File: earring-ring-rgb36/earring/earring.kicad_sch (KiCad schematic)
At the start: 44 parts, among them J1 Conn_01x04, SW1 SW_Push, U2 STM32L031G6Ux

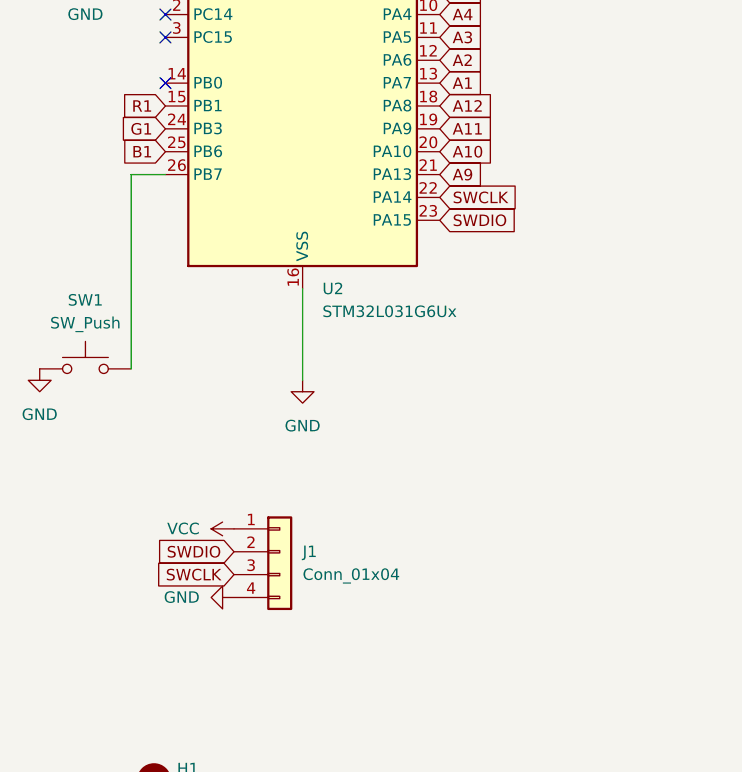
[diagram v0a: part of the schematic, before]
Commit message: earring-ring-rgb36: various fixes
* Fix problem: A9 and SWDIO were swapped
* Change program header to use a different order of pins
* various small fixes
* remove fp-info-cache which doesn't need to be committed
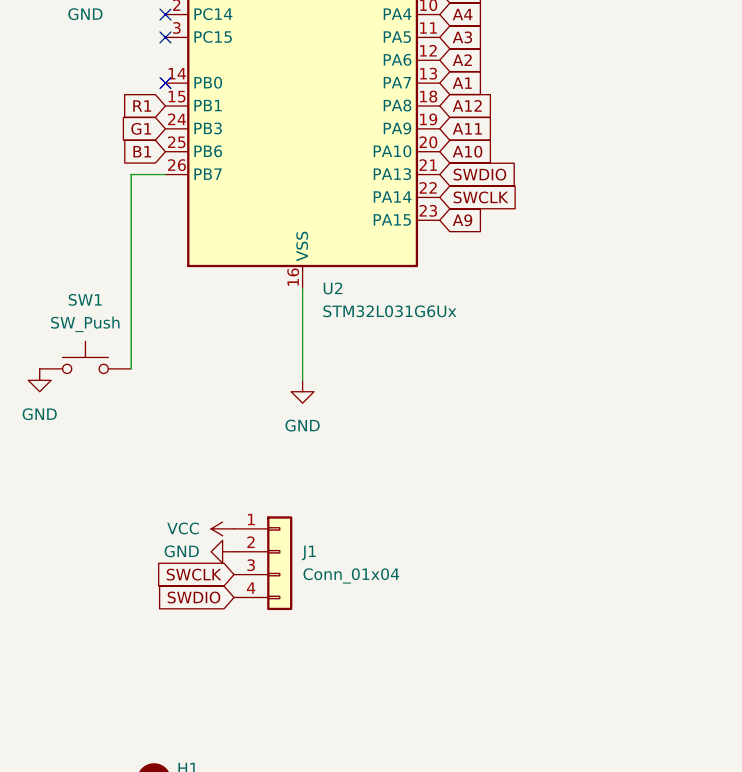
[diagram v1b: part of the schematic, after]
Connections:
- net A9: now also U2.23 (PA15); no longer U2.21 (PA13)
- net GND: now also J1.2 (Pin_2); no longer J1.4 (Pin_4)
- net SWDIO: now also J1.4 (Pin_4), U2.21 (PA13); no longer J1.2 (Pin_2), U2.23 (PA15)
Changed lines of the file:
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@@
 		)
 	)
+	(global_label "SWDIO"
+		(shape input)
+		(at 35.56 114.3 180)
+		(fields_autoplaced yes)
+		(effects
+			(font
+				(size 1.27 1.27)
+			)
+			(justify right)
+		)
+		(property "Intersheetrefs" "${INTERSHEET_REFS}"
+			(at 26.7086 114.3 0)
+			(effects
+				(font
+					(size 1.27 1.27)
+				)
+				(justify right)
+				(hide yes)
+			)
+		)
+	)
 	(global_label "A4"
 		(shape input)
@@
 		)
 	)
-	(global_label "A9"
-		(shape input)
-		(at 58.42 67.31 0)
-		(fields_autoplaced yes)
-		(effects
-			(font
-				(size 1.27 1.27)
-			)
-			(justify left)
-		)
-		(property "Intersheetrefs" "${INTERSHEET_REFS}"
-			(at 63.7033 67.31 0)
-			(effects
-				(font
-					(size 1.27 1.27)
-				)
-				(justify left)
-				(hide yes)
-			)
-		)
-	)
 	(global_label "A4"
 		(shape input)
@@
 		)
 	)
-	(global_label "A3"
+	(global_label "SWDIO"
 		(shape input)
-		(at 200.66 93.98 0)
+		(at 58.42 67.31 0)
 		(fields_autoplaced yes)
 		(effects
@@
 		)
 		(property "Intersheetrefs" "${INTERSHEET_REFS}"
-			(at 205.9433 93.98 0)
+			(at 67.2714 67.31 0)
 			(effects
 				(font
@@
 		)
 	)
-	(global_label "SWDIO"
+	(global_label "A3"
 		(shape input)
-		(at 35.56 109.22 180)
+		(at 200.66 93.98 0)
 		(fields_autoplaced yes)
 		(effects
@@
 				(size 1.27 1.27)
 			)
-			(justify right)
+			(justify left)
 		)
 		(property "Intersheetrefs" "${INTERSHEET_REFS}"
-			(at 26.7086 109.22 0)
+			(at 205.9433 93.98 0)
 			(effects
 				(font
 					(size 1.27 1.27)
 				)
-				(justify right)
+				(justify left)
 				(hide yes)
 			)
@@
 		)
 	)
-	(global_label "SWDIO"
-		(shape input)
-		(at 58.42 72.39 0)
-		(fields_autoplaced yes)
-		(effects
-			(font
-				(size 1.27 1.27)
-			)
-			(justify left)
-		)
-		(property "Intersheetrefs" "${INTERSHEET_REFS}"
-			(at 67.2714 72.39 0)
-			(effects
-				(font
-					(size 1.27 1.27)
-				)
-				(justify left)
-				(hide yes)
-			)
-		)
-	)
 	(global_label "A8"
 		(shape input)
@@
 		)
 	)
-	(global_label "SWCLK"
-		(shape input)
-		(at 35.56 111.76 180)
-		(fields_autoplaced yes)
-		(effects
-			(font
-				(size 1.27 1.27)
-			)
-			(justify right)
-		)
-		(property "Intersheetrefs" "${INTERSHEET_REFS}"
-			(at 26.3458 111.76 0)
-			(effects
-				(font
-					(size 1.27 1.27)
-				)
-				(justify right)
-				(hide yes)
-			)
-		)
-	)
 	(global_label "A8"
 		(shape input)
@@
 		)
 	)
+	(global_label "A9"
+		(shape input)
+		(at 58.42 72.39 0)
+		(fields_autoplaced yes)
+		(effects
+			(font
+				(size 1.27 1.27)
+			)
+			(justify left)
+		)
+		(property "Intersheetrefs" "${INTERSHEET_REFS}"
+			(at 63.7033 72.39 0)
+			(effects
+				(font
+					(size 1.27 1.27)
+				)
+				(justify left)
+				(hide yes)
+			)
+		)
+	)
 	(global_label "A1"
 		(shape input)
@@
 		)
 	)
+	(global_label "SWCLK"
+		(shape input)
+		(at 35.56 111.76 180)
+		(fields_autoplaced yes)
+		(effects
+			(font
+				(size 1.27 1.27)
+			)
+			(justify right)
+		)
+		(property "Intersheetrefs" "${INTERSHEET_REFS}"
+			(at 26.3458 111.76 0)
+			(effects
+				(font
+					(size 1.27 1.27)
+				)
+				(justify right)
+				(hide yes)
+			)
+		)
+	)
 	(global_label "A4"
 		(shape input)
@@
 	)
 	(symbol
+		(lib_id "power:GND")
+		(at 35.56 109.22 270)
+		(unit 1)
+		(exclude_from_sim no)
+		(in_bom yes)
+		(on_board yes)
+		(dnp no)
+		(fields_autoplaced yes)
+		(property "Reference" "#PWR03"
+			(at 29.21 109.22 0)
+			(effects
+				(font
+					(size 1.27 1.27)
+				)
+				(hide yes)
+			)
+		)
+		(property "Value" "GND"
+			(at 31.75 109.2199 90)
+			(effects
+				(font
+					(size 1.27 1.27)
+				)
+				(justify right)
+			)
+		)
+		(property "Footprint" ""
+			(at 35.56 109.22 0)
+			(effects
+				(font
+					(size 1.27 1.27)
+				)
+				(hide yes)
+			)
+		)
+		(property "Datasheet" ""
+			(at 35.56 109.22 0)
+			(effects
+				(font
+					(size 1.27 1.27)
+				)
+				(hide yes)
+			)
+		)
+		(property "Description" "Power symbol creates a global label with name \"GND\" , ground"
+			(at 35.56 109.22 0)
+			(effects
+				(font
+					(size 1.27 1.27)
+				)
+				(hide yes)
+			)
+		)
+		(pin "1"
+		)
+		(instances
+			(project "earring"
+				(path "/5b672b97-2486-4be1-9927-7141d9b63fb2"
+					(reference "#PWR03")
+					(unit 1)
+				)
+			)
+		)
+	)
+	(symbol
 		(lib_id "power:VCC")
 		(at 77.47 22.86 0)
@@
 					(unit 1)
 				)
-			)
-		)
-	)
-	(symbol
-		(lib_id "power:GND")
-		(at 35.56 114.3 270)
-		(unit 1)
-		(exclude_from_sim no)
-		(in_bom yes)
-		(on_board yes)
-		(dnp no)
-		(fields_autoplaced yes)
-		(property "Reference" "#PWR03"
-			(at 29.21 114.3 0)
-			(effects
-				(font
-					(size 1.27 1.27)
-				)
-				(hide yes)
-			)
-		)
-		(property "Value" "GND"
-			(at 31.75 114.2999 90)
-			(effects
-				(font
-					(size 1.27 1.27)
-				)
-				(justify right)
-			)
-		)
-		(property "Footprint" ""
-			(at 35.56 114.3 0)
-			(effects
-				(font
-					(size 1.27 1.27)
-				)
-				(hide yes)
-			)
-		)
-		(property "Datasheet" ""
-			(at 35.56 114.3 0)
-			(effects
-				(font
-					(size 1.27 1.27)
-				)
-				(hide yes)
-			)
-		)
-		(property "Description" "Power symbol creates a global label with name \"GND\" , ground"
-			(at 35.56 114.3 0)
-			(effects
-				(font
-					(size 1.27 1.27)
-				)
-				(hide yes)
-			)
-		)
-		(pin "1"
-		)
-		(instances
-			(project ""
-				(path "/5b672b97-2486-4be1-9927-7141d9b63fb2"
-					(reference "#PWR03")
-					(unit 1)
-				)

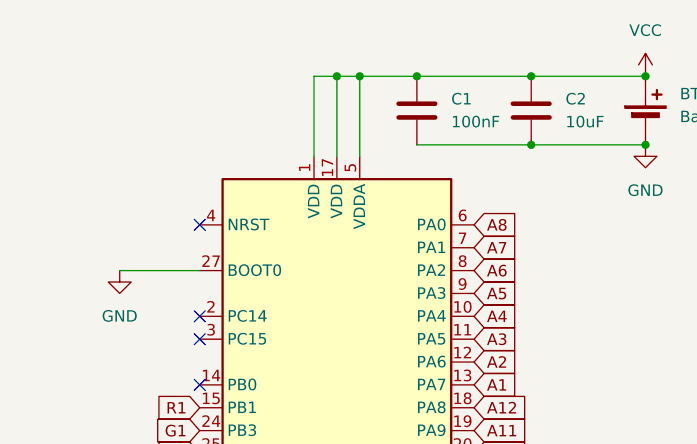
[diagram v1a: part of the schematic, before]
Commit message: earring-ring-rgb36: small changes
* use a single capacitor instead of two (apparently that's just fine)
* add a NRST test point
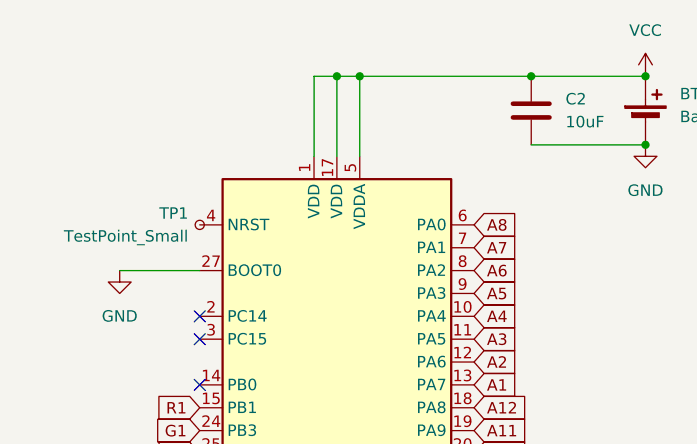
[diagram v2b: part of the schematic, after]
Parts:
- removed C1: 100nF, Capacitor_SMD:C_0402_1005Metric, symbol Device:C
- added TP1: TestPoint_Small, Custom:TestPoint_1.0x1.0mm, symbol Connector:TestPoint_Small
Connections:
- net at U2.4 (NRST): now also TP1.1
- no-connect marks 4 -> 3
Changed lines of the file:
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@@
 	)
 	(junction
-		(at 64.77 30.48)
-		(diameter 0)
-		(color 0 0 0 0)
-	)
-	(junction
 		(at 77.47 30.48)
 		(diameter 0)
 		(color 0 0 0 0)
 	)
-	(junction
-		(at 52.07 22.86)
-		(diameter 0)
-		(color 0 0 0 0)
-	)
 	(no_connect
 		(at 27.94 49.53)
@@
 	)
 	(no_connect
-		(at 27.94 39.37)
-	)
-	(no_connect
 		(at 27.94 57.15)
 	)
@@
 	(wire
 		(pts
-			(xy 52.07 22.86) (xy 64.77 22.86)
-		)
-		(stroke
-			(width 0)
-			(type default)
-		)
-	)
-	(wire
-		(pts
 			(xy 40.64 22.86) (xy 40.64 31.75)
 		)
@@
 	(wire
 		(pts
-			(xy 64.77 30.48) (xy 52.07 30.48)
-		)
-		(stroke
-			(width 0)
-			(type default)
-		)
-	)
-	(wire
-		(pts
 			(xy 64.77 30.48) (xy 77.47 30.48)
 		)
@@
 	(wire
 		(pts
-			(xy 45.72 22.86) (xy 52.07 22.86)
+			(xy 45.72 22.86) (xy 64.77 22.86)
 		)
 		(stroke
@@
 	)
 	(symbol
-		(lib_id "Device:C")
-		(at 52.07 26.67 0)
+		(lib_id "Device:LED_ARGB")
+		(at 105.41 73.66 90)
 		(unit 1)
 		(exclude_from_sim no)
@@
 		(dnp no)
 		(fields_autoplaced yes)
-		(property "Reference" "C1"
-			(at 55.88 25.3999 0)
+		(property "Reference" "D3"
+			(at 114.3 72.3899 90)
 			(effects
 				(font
 					(size 1.27 1.27)
 				)
-				(justify left)
+				(justify right)
 			)
 		)
-		(property "Value" "100nF"
-			(at 55.88 27.9399 0)
+		(property "Value" "LED_ARGB"
+			(at 114.3 74.9299 90)
 			(effects
 				(font
 					(size 1.27 1.27)
 				)
-				(justify left)
+				(justify right)
 			)
 		)
-		(property "Footprint" "Capacitor_SMD:C_0402_1005Metric"
-			(at 53.0352 30.48 0)
+		(property "Footprint" "Custom:NH-Z1415RGBA-SG"
+			(at 106.68 73.66 0)
 			(effects
 				(font
@@
 		)
 		(property "Datasheet" "~"
-			(at 52.07 26.67 0)
+			(at 106.68 73.66 0)
 			(effects
 				(font
@@
 			)
 		)
-		(property "Description" "Unpolarized capacitor"
-			(at 52.07 26.67 0)
+		(property "Description" "RGB LED, anode/red/green/blue"
+			(at 105.41 73.66 0)
 			(effects
 				(font
@@
 			)
 		)
-		(property "LCSC" "C1525"
-			(at 52.07 26.67 0)
+		(property "LCSC" "C2874117"
+			(at 105.41 73.66 90)
 			(effects
 				(font
@@
 			)
 		)
-		(pin "1"
+		(pin "3"
 		)
 		(pin "2"
 		)
+		(pin "1"
+		)
+		(pin "4"
+		)
 		(instances
-			(project ""
+			(project "earring"
 				(path "/5b672b97-2486-4be1-9927-7141d9b63fb2"
-					(reference "C1")
+					(reference "D3")
 					(unit 1)
 				)
@@
 	)
 	(symbol
-		(lib_id "Device:LED_ARGB")
-		(at 105.41 73.66 90)
+		(lib_id "power:GND")
+		(at 77.47 30.48 0)
 		(unit 1)
 		(exclude_from_sim no)
@@
 		(dnp no)
 		(fields_autoplaced yes)
-		(property "Reference" "D3"
-			(at 114.3 72.3899 90)
-			(effects
-				(font
-					(size 1.27 1.27)
-				)
-				(justify right)
-			)
-		)
-		(property "Value" "LED_ARGB"
-			(at 114.3 74.9299 90)
+		(property "Reference" "#PWR09"
+			(at 77.47 36.83 0)
 			(effects
 				(font
 					(size 1.27 1.27)
 				)
-				(justify right)
+				(hide yes)
 			)
 		)
-		(property "Footprint" "Custom:NH-Z1415RGBA-SG"
-			(at 106.68 73.66 0)
+		(property "Value" "GND"
+			(at 77.47 35.56 0)
 			(effects
 				(font
 					(size 1.27 1.27)
 				)
-				(hide yes)
 			)
 		)
-		(property "Datasheet" "~"
-			(at 106.68 73.66 0)
+		(property "Footprint" ""
+			(at 77.47 30.48 0)
 			(effects
 				(font
@@
 			)
 		)
-		(property "Description" "RGB LED, anode/red/green/blue"
-			(at 105.41 73.66 0)
+		(property "Datasheet" ""
+			(at 77.47 30.48 0)
 			(effects
 				(font
@@
 			)
 		)
-		(property "LCSC" "C2874117"
-			(at 105.41 73.66 90)
+		(property "Description" "Power symbol creates a global label with name \"GND\" , ground"
+			(at 77.47 30.48 0)
 			(effects
 				(font
@@
 			)
 		)
-		(pin "3"
-		)
-		(pin "2"
-		)
 		(pin "1"
 		)
-		(pin "4"
-		)
 		(instances
-			(project "earring"
+			(project ""
 				(path "/5b672b97-2486-4be1-9927-7141d9b63fb2"
-					(reference "D3")
+					(reference "#PWR09")
 					(unit 1)
 				)
@@
 	)
 	(symbol
-		(lib_id "power:GND")
-		(at 77.47 30.48 0)
+		(lib_id "Connector:TestPoint_Small")
+		(at 27.94 39.37 0)
+		(mirror y)
 		(unit 1)
 		(exclude_from_sim no)
@@
 		(on_board yes)
 		(dnp no)
-		(fields_autoplaced yes)
-		(property "Reference" "#PWR09"
-			(at 77.47 36.83 0)
+		(property "Reference" "TP1"
+			(at 26.67 38.0999 0)
 			(effects
 				(font
 					(size 1.27 1.27)
 				)
-				(hide yes)
+				(justify left)
 			)
 		)
-		(property "Value" "GND"
-			(at 77.47 35.56 0)
+		(property "Value" "TestPoint_Small"
+			(at 26.67 40.6399 0)
 			(effects
 				(font
 					(size 1.27 1.27)
 				)
+				(justify left)
 			)
 		)
-		(property "Footprint" ""
-			(at 77.47 30.48 0)
+		(property "Footprint" "Custom:TestPoint_1.0x1.0mm"
+			(at 22.86 39.37 0)
 			(effects
 				(font
@@
 			)
 		)
-		(property "Datasheet" ""
-			(at 77.47 30.48 0)
+		(property "Datasheet" "~"
+			(at 22.86 39.37 0)
 			(effects
 				(font
@@
 			)
 		)
-		(property "Description" "Power symbol creates a global label with name \"GND\" , ground"
-			(at 77.47 30.48 0)
+		(property "Description" "test point"
+			(at 27.94 39.37 0)
 			(effects
 				(font
@@
 			(project ""
 				(path "/5b672b97-2486-4be1-9927-7141d9b63fb2"
-					(reference "#PWR09")
+					(reference "TP1")
 					(unit 1)
 				)
